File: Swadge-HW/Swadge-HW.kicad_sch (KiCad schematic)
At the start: 96 parts, among them J1 SAO, J2 PJ-307C, J3 PGM, P1 USB_C_Plug_USB2.0, Q1 Q_PMOS_GSD, SW1 YTS-D003-1A, SW2 YTS-D003-1A, SW3 YTS-D003-1A, SW4 YTS-D003-1A, SW5 YTS-D003-1A, SW6 YTS-D003-1A, SW7 B3FS-4002P, SW8 B3FS-4002P, SW9 SW_SPDT_1825232-1, U1 ESP32-S2-MINI-1, U2 RB017A1505A, U3 MT3410, U5 RB017A1505A_Connector, U6 LSM6DSL, U7 GENERIC_LDO_2.8, U8 FM8002A, U9 INGHAi_GSPK2307P-8R1W

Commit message: fix short on garbotnik, schematic parity
C26 pointed at different part on schematic
garbotnik was shorted to ground
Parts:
- C26: footprint Swadge_Parts:C_Radial_D4_L5.4_P3.321 -> Swadge_Parts:C_Radial_D6.3_L5.8_P5.34
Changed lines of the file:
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@@
 			)
 		)
-		(property "Footprint" "Swadge_Parts:C_Radial_D4_L5.4_P3.321"
+		(property "Footprint" "Swadge_Parts:C_Radial_D6.3_L5.8_P5.34"
 			(at 166.37 193.04 0)
 			(effects

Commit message: final_updated_final_no_this_one
DNP U10, C21
Fixing my dyslexia in the quote information
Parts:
- C21, U10: now not fitted; now left out of the parts list
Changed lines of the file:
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@@
 		(unit 1)
 		(exclude_from_sim no)
-		(in_bom yes)
-		(on_board yes)
-		(dnp no)
+		(in_bom no)
+		(on_board yes)
+		(dnp yes)
 		(property "Reference" "C21"
 			(at 262.255 129.54 0)
@@
 		(unit 1)
 		(exclude_from_sim no)
-		(in_bom yes)
-		(on_board yes)
-		(dnp no)
+		(in_bom no)
+		(on_board yes)
+		(dnp yes)
 		(fields_autoplaced yes)
 		(property "Reference" "U10"

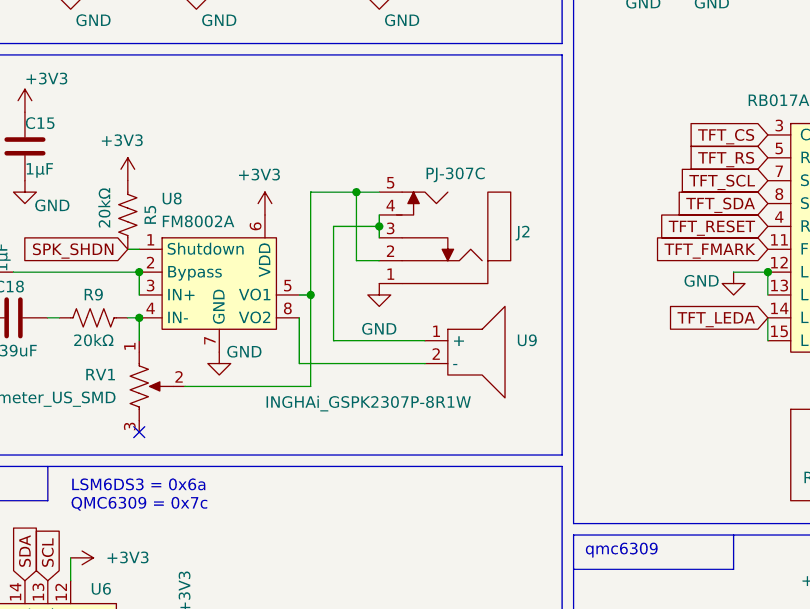
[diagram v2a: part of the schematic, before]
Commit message: Rev 1.1
add R19
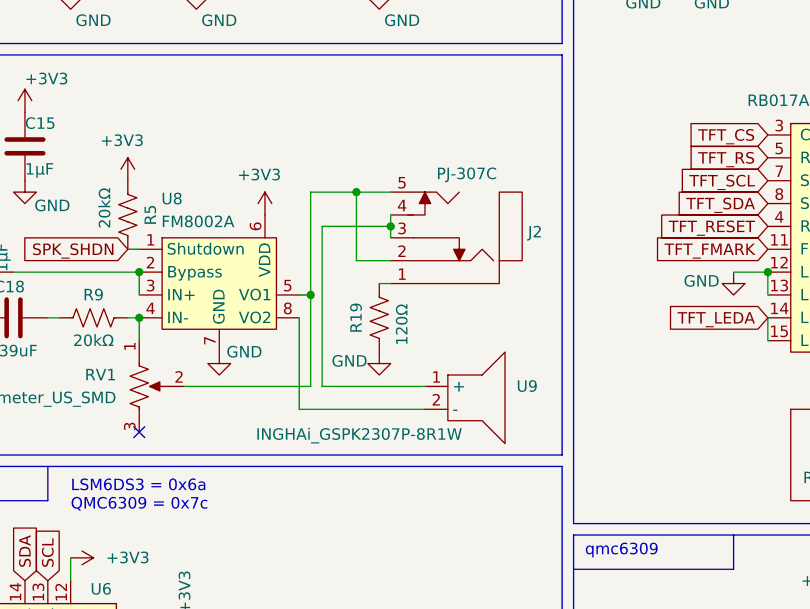
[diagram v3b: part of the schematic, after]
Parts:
- added R19: 120Ω, Swadge_Parts:R_0603_1608Metric, symbol Swadge_Parts:R_US
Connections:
- net GND: now also R19.1; no longer J2.1
- new net: J2.1, R19.2
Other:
- moved on the sheet: J2, U9
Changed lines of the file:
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@@
 	)
 	(junction
-		(at 229.87 66.04)
-		(diameter 0)
-		(color 0 0 0 0)
-	)
-	(junction
 		(at 294.64 113.03)
 		(diameter 0)
@@
 	)
 	(junction
+		(at 231.14 66.04)
+		(diameter 0)
+		(color 0 0 0 0)
+	)
+	(junction
 		(at 76.2 175.26)
 		(diameter 0)
@@
 	(wire
 		(pts
+			(xy 229.87 72.39) (xy 231.14 72.39)
+		)
+		(stroke
+			(width 0)
+			(type default)
+		)
+	)
+	(wire
+		(pts
 			(xy 189.23 71.12) (xy 203.2 71.12)
 		)
@@
 	(wire
 		(pts
-			(xy 229.87 64.77) (xy 229.87 66.04)
+			(xy 231.14 64.77) (xy 231.14 66.04)
 		)
 		(stroke
@@
 	(wire
 		(pts
-			(xy 227.33 62.23) (xy 229.87 62.23)
+			(xy 227.33 62.23) (xy 231.14 62.23)
 		)
 		(stroke
@@
 	(wire
 		(pts
-			(xy 220.98 81.28) (xy 234.95 81.28)
+			(xy 220.98 86.36) (xy 234.95 86.36)
 		)
 		(stroke
@@
 	(wire
 		(pts
-			(xy 229.87 66.04) (xy 224.79 66.04)
+			(xy 223.52 66.04) (xy 231.14 66.04)
 		)
 		(stroke
@@
 	(wire
 		(pts
-			(xy 227.33 69.85) (xy 229.87 69.85)
+			(xy 227.33 69.85) (xy 231.14 69.85)
 		)
 		(stroke
@@
 	(wire
 		(pts
-			(xy 224.79 78.74) (xy 234.95 78.74)
+			(xy 223.52 83.82) (xy 234.95 83.82)
 		)
 		(stroke
@@
 	(wire
 		(pts
-			(xy 229.87 66.04) (xy 229.87 67.31)
+			(xy 231.14 66.04) (xy 231.14 67.31)
 		)
 		(stroke
@@
 	(wire
 		(pts
-			(xy 220.98 81.28) (xy 220.98 76.2)
+			(xy 220.98 86.36) (xy 220.98 76.2)
 		)
 		(stroke
@@
 	(wire
 		(pts
-			(xy 224.79 66.04) (xy 224.79 78.74)
+			(xy 223.52 66.04) (xy 223.52 83.82)
 		)
 		(stroke
@@
 	(symbol
 		(lib_id "Swadge_Parts:R_US")
+		(at 229.87 76.2 180)
+		(unit 1)
+		(exclude_from_sim no)
+		(in_bom yes)
+		(on_board yes)
+		(dnp no)
+		(property "Reference" "R19"
+			(at 227.33 76.2 90)
+			(effects
+				(font
+					(size 1.27 1.27)
+				)
+			)
+		)
+		(property "Value" "120Ω"
+			(at 232.41 76.962 90)
+			(effects
+				(font
+					(size 1.27 1.27)
+				)
+			)
+		)
+		(property "Footprint" "Swadge_Parts:R_0603_1608Metric"
+			(at 228.854 75.946 90)
+			(effects
+				(font
+					(size 1.27 1.27)
+				)
+				(hide yes)
+			)
+		)
+		(property "Datasheet" "~"
+			(at 229.87 76.2 0)
+			(effects
+				(font
+					(size 1.27 1.27)
+				)
+				(hide yes)
+			)
+		)
+		(property "Description" ""
+			(at 229.87 76.2 0)
+			(effects
+				(font
+					(size 1.27 1.27)
+				)
+				(hide yes)
+			)
+		)
+		(property "Cost100" "10"
+			(at 278.13 30.48 0)
+			(effects
+				(font
+					(size 1.27 1.27)
+				)
+				(hide yes)
+			)
+		)
+		(property "Digikey" "~"
+			(at 278.13 30.48 0)
+			(effects
+				(font
+					(size 1.27 1.27)
+				)
+				(hide yes)
+			)
+		)
+		(property "Substitutable" "Y"
+			(at 278.13 30.48 0)
+			(effects
+				(font
+					(size 1.27 1.27)
+				)
+				(hide yes)
+			)
+		)
+		(property "LCSC" "C313655"
+			(at 229.87 76.2 0)
+			(effects
+				(font
+					(size 1.27 1.27)
+				)
+				(hide yes)
+			)
+		)
+		(property "Cost @ 2.5k" "0.0007"
+			(at 229.87 76.2 0)
+			(effects
+				(font
+					(size 1.27 1.27)
+				)
+				(hide yes)
+			)
+		)
+		(pin "1"
+		)
+		(pin "2"
+		)
+		(instances
+			(project "Swadge-HW"
+				(path "/770c762f-3a30-4864-b7da-de353459cdd6"
+					(reference "R19")
+					(unit 1)
+				)
+			)
+		)
+	)
+	(symbol
+		(lib_id "Swadge_Parts:R_US")
 		(at 208.28 116.84 180)
 		(unit 1)
@@
 	(symbol
 		(lib_id "Swadge_Parts:INGHAi_GSPK2307P-8R1W")
-		(at 237.49 80.01 0)
+		(at 237.49 85.09 0)
 		(unit 1)
 		(exclude_from_sim no)
@@
 		(dnp no)
 		(property "Reference" "U9"
-			(at 245.11 78.7399 0)
+			(at 245.11 83.8199 0)
 			(effects
 				(font
@@
 		)
 		(property "Value" "INGHAi_GSPK2307P-8R1W"
-			(at 217.17 85.5979 0)
+			(at 216.154 89.154 0)
 			(effects
 				(font
@@
 		)
 		(property "Footprint" "Swadge_Parts:INGHAi GSPK2308P-8R0.5W"
-			(at 237.49 72.39 0)
+			(at 237.49 77.47 0)
 			(effects
 				(font
@@
 		)
 		(property "Datasheet" "https://www.lcsc.com/datasheet/lcsc_datasheet_2007231713_INGHAi-GSPK2307P-8R1W_C530531.pdf"
-			(at 237.49 69.85 0)
+			(at 237.49 74.93 0)
 			(effects
 				(font
@@
 		)
 		(property "Description" ""
-			(at 237.49 80.01 0)
+			(at 237.49 85.09 0)
 			(effects
 				(font
@@
 		)
 		(property "Notes" ""
-			(at 237.49 67.31 0)
+			(at 237.49 72.39 0)
 			(effects
 				(font
@@
 		)
 		(property "Digikey" "102-2500-ND"
-			(at 237.49 64.77 0)
+			(at 237.49 69.85 0)
 			(effects
 				(font
@@
 		)
 		(property "Substitutable" "Y"
-			(at 237.49 59.69 0)
+			(at 237.49 64.77 0)
 			(effects
 				(font
@@
 		)
 		(property "Cost100" "54"
-			(at 237.49 62.23 0)
+			(at 237.49 67.31 0)
 			(effects
 				(font
@@
 		)
 		(property "LCSC" "C530531"
-			(at 237.49 80.01 0)
+			(at 237.49 85.09 0)
 			(effects
 				(font
@@
 		)
 		(property "Cost @ 2.5k" "0.412"
-			(at 237.49 80.01 0)
+			(at 237.49 85.09 0)
 			(effects
 				(font
@@
 	(symbol
 		(lib_id "Swadge_Parts:PJ-307C")
-		(at 232.41 67.31 180)
+		(at 233.68 67.31 180)
 		(unit 1)
 		(exclude_from_sim no)
@@
 		(dnp no)
 		(property "Reference" "J2"
-			(at 245.11 66.6749 0)
+			(at 246.38 66.6749 0)
 			(effects
 				(font
@@
 		)
 		(property "Value" "PJ-307C"
-			(at 234.95 60.198 0)
+			(at 236.22 60.198 0)
 			(effects
 				(font
@@
 		)
 		(property "Footprint" "Swadge_Parts:PJ-307C"
-			(at 232.41 55.245 0)
+			(at 233.68 55.245 0)
 			(effects
 				(font
@@
 		)
 		(property "Datasheet" "https://datasheet.lcsc.com/lcsc/1811040611_BOOMELE-Boom-Precision-Elec-PJ-307C_C16684.pdf"
-			(at 232.41 59.69 0)
+			(at 233.68 59.69 0)
 			(effects
 				(font
@@
 		)
 		(property "Description" ""
-			(at 232.41 67.31 0)
+			(at 233.68 67.31 0)
 			(effects
 				(font
@@
 		)
 		(property "LCSC" "C16684"
-			(at 232.41 57.15 0)
+			(at 233.68 57.15 0)
 			(effects
 				(font
@@
 		)
 		(property "Cost @ 2.5k" "0.0261"
-			(at 232.41 67.31 0)
+			(at 233.68 67.31 0)
 			(effects
 				(font
@@
 	(symbol
 		(lib_id "Swadge_Parts:GND")
-		(at 229.87 72.39 0)
+		(at 229.87 80.01 0)
 		(unit 1)
 		(exclude_from_sim no)
@@
 		(on_board yes)
 		(dnp no)
-		(fields_autoplaced yes)
 		(property "Reference" "#PWR058"
-			(at 229.87 78.74 0)
+			(at 229.87 86.36 0)
 			(effects
 				(font
@@
 		)
 		(property "Value" "GND"
-			(at 229.87 77.47 0)
+			(at 226.568 81.026 0)
 			(effects
 				(font
@@
 		)
 		(property "Footprint" ""
-			(at 229.87 72.39 0)
+			(at 229.87 80.01 0)
 			(effects
 				(font
@@
 		)
 		(property "Datasheet" ""
-			(at 229.87 72.39 0)
+			(at 229.87 80.01 0)
 			(effects
 				(font
@@
 		)
 		(property "Description" ""
-			(at 229.87 72.39 0)
+			(at 229.87 80.01 0)
 			(effects
 				(font

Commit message: Paperwork makes the dream work
Schematic, render, readme updates
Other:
- company: (none) -> Magfest Inc
- title: (none) -> 2025 Super Swadge
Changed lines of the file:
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@@
 	(generator_version "8.0")
 	(paper "USLegal")
+	(title_block
+		(title "2025 Super Swadge")
+		(date "2025-02-02")
+		(company "Magfest Inc")
+	)
 	(junction
 		(at 261.62 123.19)
@@
 		)
 		(instances
-			(project ""
+			(project "Swadge-HW"
 				(path "/770c762f-3a30-4864-b7da-de353459cdd6"
 					(reference "RV1")
@@
 		)
 		(instances
-			(project ""
+			(project "Swadge-HW"
 				(path "/770c762f-3a30-4864-b7da-de353459cdd6"
 					(reference "U8")
@@
 		)
 		(instances
-			(project ""
+			(project "Swadge-HW"
 				(path "/770c762f-3a30-4864-b7da-de353459cdd6"
 					(reference "U9")
@@
 		)
 		(instances
-			(project ""
+			(project "Swadge-HW"
 				(path "/770c762f-3a30-4864-b7da-de353459cdd6"
 					(reference "J2")
@@
 		)
 		(instances
-			(project ""
+			(project "Swadge-HW"
 				(path "/770c762f-3a30-4864-b7da-de353459cdd6"
 					(reference "U10")
@@
 		)
 		(instances
-			(project ""
+			(project "Swadge-HW"
 				(path "/770c762f-3a30-4864-b7da-de353459cdd6"
 					(reference "N2")
@@
 		)
 		(instances
-			(project ""
+			(project "Swadge-HW"
 				(path "/770c762f-3a30-4864-b7da-de353459cdd6"
 					(reference "N1")

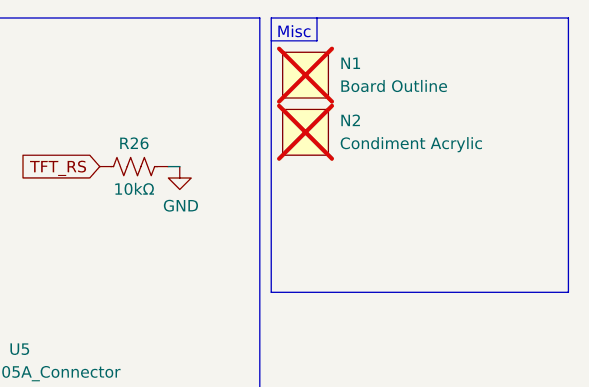
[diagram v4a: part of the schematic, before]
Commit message: Clean out last year's files (PCB, Art, Shell) Update READMEs
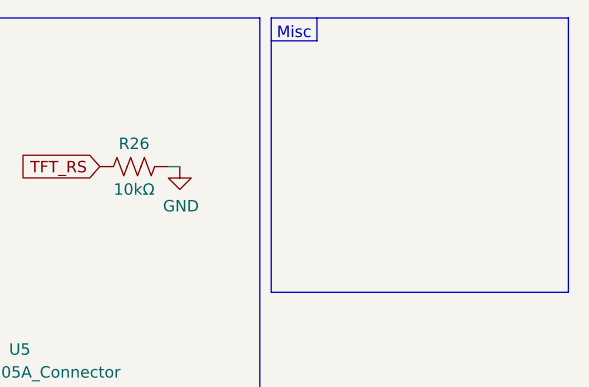
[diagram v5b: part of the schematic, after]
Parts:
- removed N1: Board Outline, Swadge_Hotdog:hotdog-outline, symbol Swadge_Parts:NULL
- removed N2: Condiment Acrylic, Swadge_Hotdog:condiment, symbol Swadge_Parts:NULL
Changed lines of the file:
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@@
-	)
-	(symbol
-		(lib_id "Swadge_Parts:NULL")
-		(at 313.69 25.4 0)
-		(unit 1)
-		(exclude_from_sim no)
-		(in_bom no)
-		(on_board yes)
-		(dnp yes)
-		(fields_autoplaced yes)
-		(property "Reference" "N2"
-			(at 317.5 24.1299 0)
-			(effects
-				(font
-					(size 1.27 1.27)
-				)
-				(justify left)
-			)
-		)
-		(property "Value" "Condiment Acrylic"
-			(at 317.5 26.6699 0)
-			(effects
-				(font
-					(size 1.27 1.27)
-				)
-				(justify left)
-			)
-		)
-		(property "Footprint" "Swadge_Hotdog:condiment"
-			(at 313.69 25.4 0)
-			(effects
-				(font
-					(size 1.27 1.27)
-				)
-				(hide yes)
-			)
-		)
-		(property "Datasheet" ""
-			(at 313.69 25.4 0)
-			(effects
-				(font
-					(size 1.27 1.27)
-				)
-				(hide yes)
-			)
-		)
-		(property "Description" ""
-			(at 313.69 25.4 0)
-			(effects
-				(font
-					(size 1.27 1.27)
-				)
-				(hide yes)
-			)
-		)
-		(instances
-			(project "Swadge-HW"
-				(path "/770c762f-3a30-4864-b7da-de353459cdd6"
-					(reference "N2")
-					(unit 1)
-				)
-			)
-		)
 	)
 	(symbol
@@
 					(unit 1)
 				)
-			)
-		)
-	)
-	(symbol
-		(lib_id "Swadge_Parts:NULL")
-		(at 313.69 19.05 0)
-		(unit 1)
-		(exclude_from_sim no)
-		(in_bom no)
-		(on_board yes)
-		(dnp yes)
-		(fields_autoplaced yes)
-		(property "Reference" "N1"
-			(at 317.5 17.7799 0)
-			(effects
-				(font
-					(size 1.27 1.27)
-				)
-				(justify left)
-			)
-		)
-		(property "Value" "Board Outline"
-			(at 317.5 20.3199 0)
-			(effects
-				(font
-					(size 1.27 1.27)
-				)
-				(justify left)
-			)
-		)
-		(property "Footprint" "Swadge_Hotdog:hotdog-outline"
-			(at 313.69 19.05 0)
-			(effects
-				(font
-					(size 1.27 1.27)
-				)
-				(hide yes)
-			)
-		)
-		(property "Datasheet" ""
-			(at 313.69 19.05 0)
-			(effects
-				(font
-					(size 1.27 1.27)
-				)
-				(hide yes)
-			)
-		)
-		(property "Description" ""
-			(at 313.69 19.05 0)
-			(effects
-				(font
-					(size 1.27 1.27)
-				)
-				(hide yes)
-			)
-		)
-		(instances
-			(project "Swadge-HW"
-				(path "/770c762f-3a30-4864-b7da-de353459cdd6"
-					(reference "N1")
-					(unit 1)
-				)

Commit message: Add LED matrix and CH32v003 Repopulate magnometer and associated components DNP giant capacitor Change sheet size to 11x17 Change labels to 2026
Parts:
- added D13, D14, D15, D16, D17, D18, D19, D20, D21, D22, D23, D24, D25, D26, D27, D28, D29, D30, D31, D32, D33, D34, D35, D36, D37, D38, D39, D40, D41, D42, D43, D44, D45, D46, D47, D48, D49, D50, D51, D52, D53, D54, D55, D56, D57, D58, D59, D60, D61, D62, D63, D64, D65, D66, D67, D68, D69, D70, D71, D72, D73, D74, D75, D76, D77, D78, D79, D80, D81, D82, D83, D84: P2-1206RTCS2-0.9T-F, LED_SMD:LED_1206_3216Metric_ReverseMount_Hole1.8x2.4mm, symbol LED:LD271
- added R20, R23, R29, R30, R31, R32, R33, R34: TBD, Swadge_Parts:R_0603_1608Metric, symbol Swadge_Parts:R_US
- added U11: CH32V003F4U6, Swadge_Parts:QFN-20-1EP_3x3mm_P0.4mm_EP1.65x1.65mm, symbol Swadge_Parts:CH32V003F4U6
- C21, U10: now fitted; now in the parts list
- C26: now not fitted; now left out of the parts list
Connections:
- net +3V3: now also U11.6 (VDD)
- net GND: now also U11.21 (GND), U11.4 (VSS)
- net GPIO42: now also U11.15 (PD1/SWIO/AETR/T1CH3/SCL/URX)
- new net: R32.1, U11.12 (PC5/SCK/T1ETR/T2CH1ETR/SCL/UCK/T1CH3)
- new net: R33.1, U11.13 (PC6/MOSI/T1CH1CH3/UCTS/SDA)
- new net: R30.2, U11.10 (PC3/T1CH3/T1CHIN/UCTS)
- new net: R29.2, U11.9 (PC2/SCL/URTS/T1BKIN/AETR/T2CH2/T1ETR)
- new net: R31.1, U11.11 (PC4/A2/T1CH4/MCO/T1CH1CH2N)
- new net: R20.2, U11.7 (PC0/T2CH3/UTX/NSS/T1CH3)
- new net: R34.1, U11.14 (PC7/MISO/T1CH2/T2CH2/URTS)
- new net: R23.2, U11.8 (PC1/SDA/NSS/T2CH4/T2CH1ETR/T1BKIN/URX)
- new net C1: D13.2 (A), D14.2 (A), D15.2 (A), D16.2 (A), D17.2 (A), D18.2 (A), D19.2 (A), D20.2 (A), U11.1 (PD7/NRST/T2CH4/OPP1/UCK)
- new net C2: D21.2 (A), D22.2 (A), D23.2 (A), D24.2 (A), D25.2 (A), D26.2 (A), D27.2 (A), D28.2 (A), U11.2 (PA1/OSCI/A1/T1CH2/OPN0)
- new net C3: D29.2 (A), D30.2 (A), D31.2 (A), D32.2 (A), D33.2 (A), D34.2 (A), D35.2 (A), D36.2 (A), U11.3 (PA2/OSCO/A0/T1CH2N/OPP0/AETR2)
- new net C4: D37.2 (A), D38.2 (A), D39.2 (A), D40.2 (A), D41.2 (A), D42.2 (A), D43.2 (A), D44.2 (A), U11.5 (PD0/T1CH1N/OPN1/SDA/UTX)
- new net C5: D45.2 (A), D46.2 (A), D47.2 (A), D48.2 (A), D49.2 (A), D50.2 (A), D51.2 (A), D52.2 (A), U11.16 (PD2/A3/T1CH1/T2CH3/T1CH2N)
- new net C6: D53.2 (A), D54.2 (A), D55.2 (A), D56.2 (A), D57.2 (A), D58.2 (A), D59.2 (A), D60.2 (A), U11.17 (PD3/A4/T2CH2/AETR/UCTS/T1CH4)
- new net C7: D61.2 (A), D62.2 (A), D63.2 (A), D64.2 (A), D65.2 (A), D66.2 (A), D67.2 (A), D68.2 (A), U11.18 (PD4/A7/UCK/T2CH1ETR/OPO/T1CH4ETR)
- new net C8: D69.2 (A), D70.2 (A), D71.2 (A), D72.2 (A), D73.2 (A), D74.2 (A), D75.2 (A), D76.2 (A), U11.19 (PD5/A5/UTX/T2CH4/URX)
- new net C9: D77.2 (A), D78.2 (A), D79.2 (A), D80.2 (A), D81.2 (A), D82.2 (A), D83.2 (A), D84.2 (A), U11.20 (PD6/A7/URX/T2CH3/UTX)
- new net R1: D13.1 (K), D21.1 (K), D29.1 (K), D37.1 (K), D45.1 (K), D53.1 (K), D61.1 (K), D69.1 (K), D77.1 (K), R20.1
- new net R2: D14.1 (K), D22.1 (K), D30.1 (K), D38.1 (K), D46.1 (K), D54.1 (K), D62.1 (K), D70.1 (K), D78.1 (K), R23.1
- new net R3: D15.1 (K), D23.1 (K), D31.1 (K), D39.1 (K), D47.1 (K), D55.1 (K), D63.1 (K), D71.1 (K), D79.1 (K), R29.1
- new net R4: D16.1 (K), D24.1 (K), D32.1 (K), D40.1 (K), D48.1 (K), D56.1 (K), D64.1 (K), D72.1 (K), D80.1 (K), R30.1
- new net R5: D17.1 (K), D25.1 (K), D33.1 (K), D41.1 (K), D49.1 (K), D57.1 (K), D65.1 (K), D73.1 (K), D81.1 (K), R31.2
- new net R6: D18.1 (K), D26.1 (K), D34.1 (K), D42.1 (K), D50.1 (K), D58.1 (K), D66.1 (K), D74.1 (K), D82.1 (K), R32.2
- new net R7: D19.1 (K), D27.1 (K), D35.1 (K), D43.1 (K), D51.1 (K), D59.1 (K), D67.1 (K), D75.1 (K), D83.1 (K), R33.2
- new net R8: D20.1 (K), D28.1 (K), D36.1 (K), D44.1 (K), D52.1 (K), D60.1 (K), D68.1 (K), D76.1 (K), D84.1 (K), R34.2
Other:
- note added: "COLUMN 1"
- note added: "COLUMN 2"
- note added: "COLUMN 3"
- note added: "COLUMN 4"
- note added: "COLUMN 5"
- note added: "COLUMN 6"
- note added: "COLUMN 7"
- note added: "COLUMN 8"
- note added: "COLUMN 9"
- note added: "ELECTRICAL POSITION VS PHYSICAL POSITION"
- note added: "LED Matrix"
- note added: "LEFT EYE ROWS 1-6 COLS 1-6 ORIGIN IN TOP LEFT"
- note added: "RIGHT EYE ROW 1-6 COLS 7-12 ORIGIN IN TOP LEFT"
- title: 2025 Super Swadge -> 2026 Super Swadge
- moved on the sheet: C10, C11, C12, C13, C16, C19, C22, C23, C25, C7, D10, J1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

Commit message: preliminary layout
placed most of the important bits
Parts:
- C1, C11, C14, C15, C17, C19, C24, C4, C5, C6, C8: value 1μF -> C
- C10, C13, C16, C23, C25, C3: value 0.1μF -> C
- C12, C2, C20, C22, C7: value 22μF -> C
- C18: value 0.39uF -> C
- C21: value 2.2μF -> C
- C26: value 470μF -> C_Polarized_US; now in the parts list
- C9: value 4.7nF -> C
- D1, D2, D3, D4, D5, D6, D7, D8, D9: value LC8812B-4020 -> SK6812-SIDE-A; footprint Swadge_Parts:4020PAD -> Swadge_Parts:SK6812_SIDE_2; Digikey (none) -> 1528-4691-ND; LCSC C5446701 -> C2890037
- D13, D14, D15, D16, D17, D18, D19, D20, D21, D22, D23, D24, D25, D26, D27, D28, D29, D30, D31, D32, D33, D34, D35, D36, D37, D38, D39, D40, D41, D42, D43, D44, D45, D46, D47, D48, D49, D50, D51, D52, D53, D54, D55, D56, D57, D58, D59, D60, D61, D62, D63, D64, D65, D66, D67, D68, D69, D70, D71, D72, D73, D74, D75, D76, D77, D78, D79, D80, D81, D82, D83, D84: value P2-1206RTCS2-0.9T-F -> A-SP192GB1D-A02-4T; footprint LED_SMD:LED_1206_3216Metric_ReverseMount_Hole1.8x2.4mm -> LED_SMD:LED_0603_1608Metric; symbol LED:LD271 -> Swadge_Parts:A-SP192GB1D-A02-4T; LCSC C2827254 -> C5355458
- J1: value SAO -> Conn_02x03_Odd_Even; footprint Swadge_Parts:PinSocket_2x03_P2.54mm_Vertical -> Swadge_Parts:PinHeader_2x03_P2.54mm_Vertical
- J3: value PGM -> Conn_01x05_Male; LCSC (none) -> C390683; now in the parts list
- L1: value 33uH_500mA -> L; footprint Swadge_Parts:L_1210_3225Metric -> Swadge_Parts:L_0603_1608Metric
- L3: value 2.2uH -> L; footprint Swadge_Parts:L_1008_2520Metric -> Swadge_Parts:L_0603_1608Metric
- MK1: footprint Swadge_Parts:INGHAi_MIC_GMI4013S-2C58DB -> Swadge_Parts:INGHAi-Microphone-4mm; LCSC C529870 -> C529885
- R1, R22, R24, R26, R7: value 10kΩ -> R_US
- R10, R11, R12, R15, R16, R17: value 510Ω -> R_US
- R13, R14, R2, R4, R8: value 33Ω -> R_US
- R18, R27, R28, R6: value 5.1kΩ -> R_US
- R19: value 120Ω -> R_US
- R20, R23, R29, R30, R31, R32, R33, R34: value TBD -> R_US
- R21, R25: value 43kΩ -> R_US
- R3: value 12kΩ -> R_US
- R5, R9: value 20kΩ -> R_US
- RV1: LCSC C3020613 -> C470765
- SW7, SW8: LCSC C2929546 -> C455218; Notes Use standard 12mmx12mm SMT box tactile buttons with flat top. Similar to TS-1103S-B-A. -> Use standard 12mmx12mm SMT box tactile buttons with flat top. Similar to TL3300DF160Q.
- U3: value MT3410 -> M3410; Substitutable Y -> Yes
- U4: footprint Swadge_Parts:Touch_Teeth_5b -> Swadge_Parts:Touch_Teeth_5; now in the parts list
- U7: value GENERIC_LDO_2.8 -> GENERIC_LDO_GOI
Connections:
- net +3V3: no longer C11.1, C15.1, C16.1, C17.1, C2.1, C24.1, C26.1, C3.1, C4.1, C5.1, C6.1, C8.1, D1.2 (VDD), D2.2 (VDD), D3.2 (VDD), D4.2 (VDD), D5.2 (VDD), D6.2 (VDD), D7.2 (VDD), D8.2 (VDD), D9.2 (VDD), J1.1 (Pin_1), L3.1, Q1.2 (S), R1.1, R2.2, R25.2, R5.1, R7.1, U1.3 (3V3), U11.6 (VDD), U7.3 (IN), U8.6 (VDD)
- new net +3.3V: C11.1, C15.1, C16.1, C17.1, C2.1, C24.1, C26.1, C3.1, C4.1, C5.1, C6.1, C8.1, D1.2 (VDD), D2.2 (VDD), D3.2 (VDD), D4.2 (VDD), D5.2 (VDD), D6.2 (VDD), D7.2 (VDD), D8.2 (VDD), D9.2 (VDD), J1.1 (Pin_1), L3.1, Q1.2 (S), R1.1, R2.2, R25.2, R5.1, R7.1, U1.3 (3V3), U11.6 (VDD), U7.3 (IN), U8.6 (VDD)

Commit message: Half the routing done
Do you think God stays in heaven because he, too, lives in fear of what he's created here on earth?
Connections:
- net +3.3V: now also C10.1, R8.2, U6.12 (CS), U6.5 (VDDIO)
- net +3V3: no longer C10.1, R8.2, U6.12 (CS), U6.5 (VDDIO)
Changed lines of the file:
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@@
 	(wire
 		(pts
-			(xy 111.76 236.22) (xy 115.57 236.22)
+			(xy 101.6 236.22) (xy 115.57 236.22)
 		)
 		(stroke
@@
 	(symbol
 		(lib_id "Swadge_Parts:GND")
-		(at 111.76 236.22 0)
+		(at 101.6 236.22 0)
 		(unit 1)
 		(exclude_from_sim no)
@@
 		(dnp no)
 		(property "Reference" "#PWR10"
-			(at 111.76 242.57 0)
+			(at 101.6 242.57 0)
 			(effects
 				(font
@@
 		)
 		(property "Value" "GND"
-			(at 111.76 240.03 0)
+			(at 101.6 240.03 0)
 			(effects
 				(font
@@
 		)
 		(property "Footprint" ""
-			(at 111.76 236.22 0)
+			(at 101.6 236.22 0)
 			(effects
 				(font
@@
 		)
 		(property "Datasheet" ""
-			(at 111.76 236.22 0)
+			(at 101.6 236.22 0)
 			(effects
 				(font
@@
 		)
 		(property "Description" "Power symbol creates a global label with name \"GND\" , ground"
-			(at 111.76 236.22 0)
+			(at 101.6 236.22 0)
 			(effects
 				(font
@@
 			)
 		)
-		(property "Value" "+3V3"
+		(property "Value" "+3.3V"
 			(at 202.184 250.19 0)
 			(effects
@@
 			)
 		)
-		(property "Value" "+3V3"
+		(property "Value" "+3.3V"
 			(at 214.376 222.25 0)
 			(effects
@@
 			)
 		)
-		(property "Value" "+3V3"
+		(property "Value" "+3.3V"
 			(at 238.76 236.474 0)
 			(effects
@@
 			)
 		)
-		(property "Value" "+3V3"
+		(property "Value" "+3.3V"
 			(at 223.52 228.854 0)
 			(effects
